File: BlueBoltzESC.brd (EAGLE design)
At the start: 207.3 x 74.4 mm, 86 parts, among them IC1 7805TV, Q1 BD679, Q2 BD679, Q3 BD679, Q4 IRLZ44Z, Q5 IRLZ44Z, Q6 IRLZ44Z, Q7 IRLZ44Z, Q8 IRLZ44Z, Q9 IRLZ44Z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

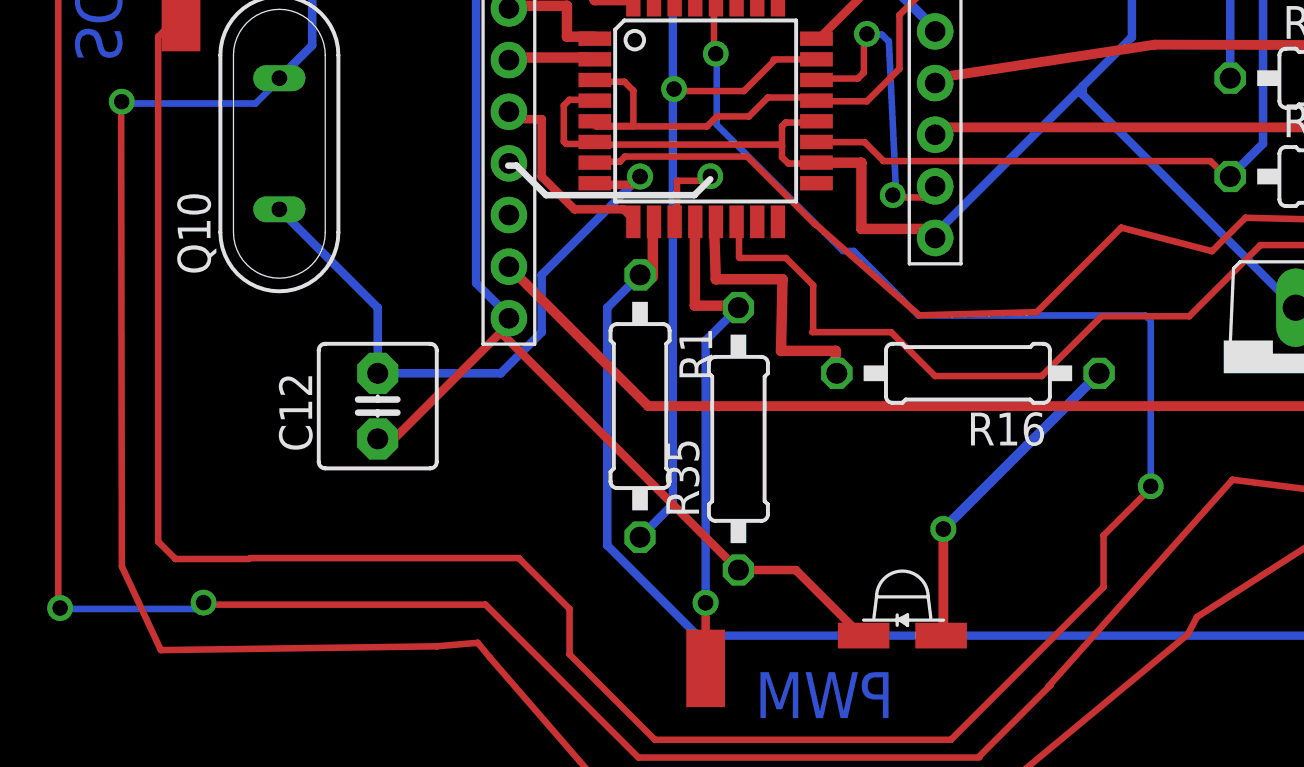
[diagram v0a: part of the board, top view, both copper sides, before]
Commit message: Version 1.1 For BlueBoltzESC Board
In this Version, The board is updated with a single board footprint, which minimizes hassles...
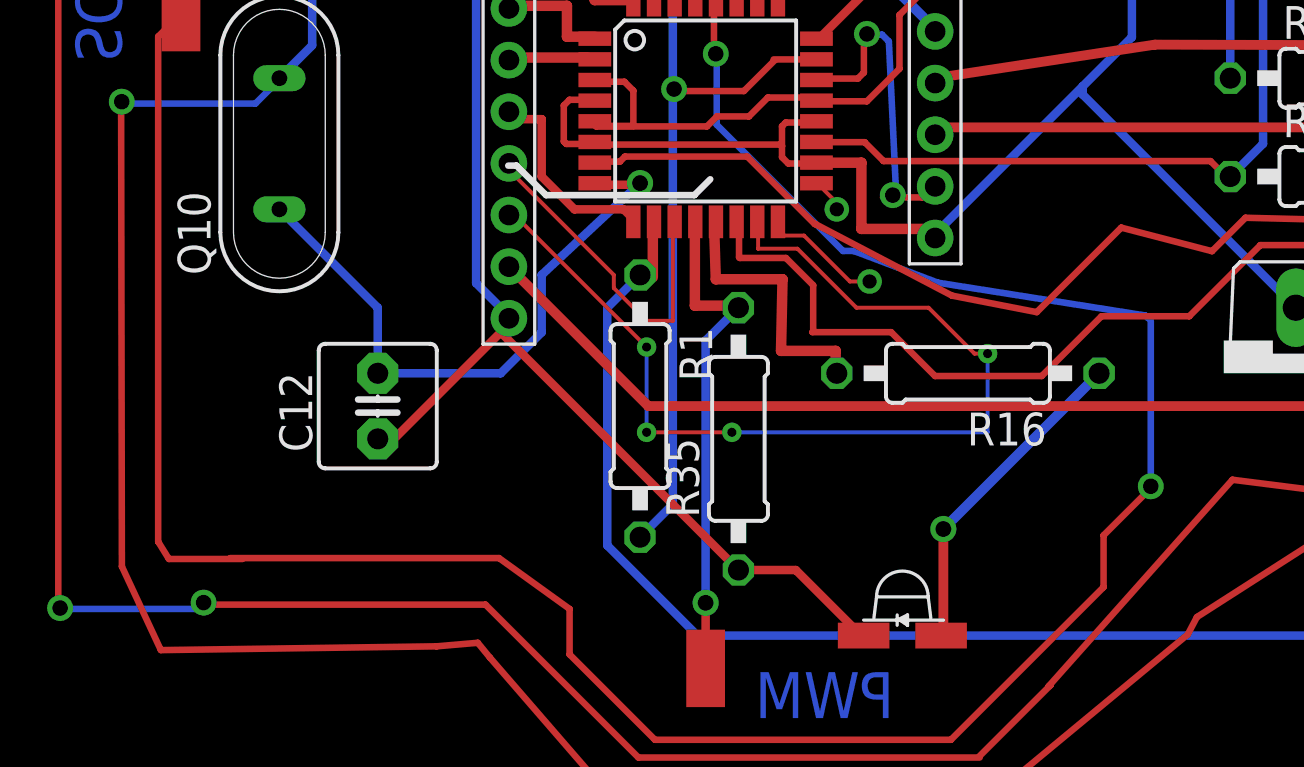
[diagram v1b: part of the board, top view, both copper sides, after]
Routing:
- net N$79: track 0.00 -> 38.6 mm, vias 0 -> 4
- net N$80: track 0.00 -> 13.1 mm
- net N$82: track 0.00 -> 4.65 mm
- net N$66: track 2.92 -> 0.00 mm, vias 0 -> 1
- net N$78: track 0.00 -> 0.72 mm
- net N$57: track 22.6 -> 21.8 mm
- net N$81: track 0.00 -> 0.61 mm
- net N$61: track 129.5 -> 128.9 mm
- net N$56: track 44.1 -> 44.6 mm

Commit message: Add files via upload
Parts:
- removed IC1: 7805TV, linear:TO220V
- removed U$3: ACS7XX12-WFQFN, BR-Eagle-Library:12-WFQFN
- added 5VREG, IC2: REG1117, burr-brown:SOT223
- added IC3: ACS712ELCTR-20A-T, SamacSys_Parts:SOIC127P600X175-8N
- added J1: AVR_SPI_PROG_3X2NS, SparkFun-Connectors:2X3-NS
- added SV1: (no value), con-lstb:MA03-1
- R33: device SparkFun-Resistors:0603-RES -> varistor:R-5
- U$16, U$4: value HEADER-62MM -> (none); device BR-Eagle-Library:HEADER-2MM-6POS -> con-lsta:FE06
- U$17, U$8: value HEADER-122MM -> (none); device BR-Eagle-Library:HEADER-2MM-12POS -> con-lsta:FE12
- moved R24 189.9 mm to (94.0, 31.8)
- moved R18 189.7 mm to (94.0, 38.1)
- moved R20 172.8 mm to (62.2, 67.3)
- moved C16 168.4 mm to (63.5, 12.7)
- moved U$4 164.0 mm to (50.8, 47.0), flipped to the bottom, turned to 90 degrees
- moved U$2 157.9 mm to (33.0, 10.2), flipped to the bottom
- moved U$1 155.7 mm to (33.0, 5.08)
- moved R21 153.8 mm to (58.4, 39.4), turned to 180 degrees
- moved R36 148.2 mm to (44.5, 7.62), turned to 90 degrees
- moved C15 141.8 mm to (39.4, 12.7), turned to 90 degrees
- moved C11 137.4 mm to (41.9, 24.1), turned to 90 degrees
- moved R29 137.2 mm to (44.5, 31.8), turned to 180 degrees
- moved R33 136.5 mm to (33.0, 48.3), turned to 90 degrees
- moved U$5 127.1 mm to (5.08, 25.4)
- moved R37 126.3 mm to (58.4, 58.4), flipped to the bottom, turned to 90 degrees
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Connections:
- new net BEC+: IC2.2, SV1.2
- net CURRENT_ADC: now also U$8.4; no longer U$8.P$4
- net GND: now also IC2.1, J1.6, R33.2, SV1.3, U$4.1, U$8.1, U$8.12, U$8.2; no longer R33.1, U$4.P$1, U$8.P$1, U$8.P$12, U$8.P$2
- net L_CURRENT_ADC: now also U$17.4; no longer U$17.P$4
- net L_GND: now also 5VREG.1, U$16.1, U$17.1, U$17.12, U$17.2; no longer IC1.2, U$16.P$1, U$17.P$1, U$17.P$12, U$17.P$2
- net L_PHASE_A: now also U$16.2; no longer U$16.P$2
- net L_PHASE_B: now also U$16.3; no longer U$16.P$3
- net L_PHASE_C: now also U$16.4; no longer U$16.P$4
- net L_PWM_AH: now also U$17.5; no longer U$17.P$5
- net L_PWM_AL: now also U$17.6; no longer U$17.P$6
- net L_PWM_BH: now also U$17.7; no longer U$17.P$7
- net L_PWM_BL: now also U$17.8; no longer U$17.P$8
- net L_PWM_CH: now also U$17.9; no longer U$17.P$9
- net L_PWM_CL: now also J1.4, U$17.10; no longer U$17.P$10
- net L_TEMP_ADC: now also U$16.5; no longer U$16.P$5
- net L_VBAT: now also 5VREG.3, U$17.11; no longer IC1.1, U$17.P$11
- net MISO: now also J1.1
- net N$1: now also IC3.1, IC3.2; no longer U$3.IP+1, U$3.IP+2
- net N$13: now also IC3.5; no longer U$3.GND
- net N$14: now also IC3.8; no longer U$3.VCC
- net N$17: now also IC3.7; no longer U$3.VIOUT
- net N$8: now also IC3.3, IC3.4; no longer U$3.IP-1, U$3.IP-2
- net PHASE_A: now also U$4.2; no longer U$4.P$2
- net PHASE_B: now also U$4.3; no longer U$4.P$3
- net PHASE_C: now also U$4.4; no longer U$4.P$4
- net PWM: now also SV1.1
- net PWM_AH: now also U$8.5; no longer U$8.P$5
- net PWM_AL: now also U$8.6; no longer U$8.P$6
- net PWM_BH: now also U$8.7; no longer U$8.P$7
- net PWM_BL: now also U$8.8; no longer U$8.P$8
- net PWM_CH: now also U$8.9; no longer U$8.P$9
- net PWM_CL: now also U$8.10; no longer U$8.P$10
- net RESET: now also J1.5
- net SCK: now also J1.3
- net TEMP_ADC: now also R33.1, U$4.5; no longer R33.2, U$4.P$5
- net VBAT: now also U$8.11; no longer U$8.P$11
- net VBAT+: now also IC2.3
- net VCC5V: now also 5VREG.2, J1.2, U$16.6, U$17.3; no longer IC1.3, U$16.P$6, U$17.P$3
- net VCC5V-1: now also U$4.6; no longer U$4.P$6
- net VCC5V-2: now also U$8.3; no longer U$8.P$3
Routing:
- net VCC5V: track 104.8 -> 272.9 mm
- net N$10: track 14.5 -> 166.1 mm, vias 0 -> 2
- net L_GND: track 178.4 -> 309.3 mm, vias 0 -> 1
- net N$61: track 128.9 -> 0.00 mm, vias 1 -> 0
- net N$3: track 12.7 -> 121.8 mm, vias 1 -> 0
- net RESET: track 0.00 -> 104.9 mm, vias 0 -> 1
- net PWM: track 14.5 -> 115.7 mm, vias 1 -> 5
- net VBAT: track 118.9 -> 210.4 mm, vias 1 -> 5
- net SCL: track 6.48 -> 96.1 mm, vias 0 -> 2
- net PWM_AL: track 98.6 -> 11.5 mm
- net PWM_BH: track 124.4 -> 45.1 mm
- net PHASE_A: track 154.2 -> 77.4 mm
- net N$11: track 24.1 -> 97.9 mm, vias 1 -> 2
- net SDA: track 16.6 -> 90.4 mm, vias 2 -> 5
- net PWM_CH: track 93.8 -> 20.2 mm
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- added copper zone on layer 1, net N$18
- added copper zone on layer 16, net N$20
- removed copper zone on layer 1, net N$74
- removed copper zone on layer 16, net N$75
- removed copper zone on layer 1, net N$76
- removed copper zone on layer 16, net N$77
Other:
- board size 207.3 x 74.4 mm -> 144.8 x 87.3 mm
- board text added: "60A"
- board text added: "60A Max Load Power"
- board text added: "BlueBoltz ESC"
- board text added: "Derived From BlueESC"
- board text added: "Derived from BlueESC"
- board text added: "Industry Leading SimonK Firmware At <3"
- board text added: "Industry Leading SimonK Firmware at Heart."
- board text removed: "BluBoltz ESC 40A"
- board text removed: "GND"
- board text removed: "Logic Board"
- board text removed: "PWM"
- board text removed: "Power Driver Board"
- board text removed: "SCL"
- board text removed: "SDA"
